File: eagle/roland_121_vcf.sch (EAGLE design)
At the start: 97 parts, among them IC1 LM13700N, IC2 LM13700N, IC3 TL072P, Q1 2N3904, Q2 2N3906, Q3 2N3904, Q4 2N3904, Q5 MPF102, Q6 MPF102, Q7 MPF102, Q8 MPF102

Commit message: starting over with updated techniques
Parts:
- removed C12, C14: 22uF, rcl:CPOL-USB45181A
- removed C18: 0.1uF, rcl:C-US025-030X050
- removed C2: 470p, rcl:C-US025-030X050
- removed R1, R7: 100k, rcl:R-US_0207/7
- removed R18: 10k, rcl:R-US_0207/7
- removed R2, R3: 15k, rcl:R-US_0207/7
- removed R4: 560, rcl:R-US_0207/7
- removed R41: 68k, rcl:R-US_0207/7
- removed U$1: POWER, eurorack:POWER
- added C19: 10/25v BP, rcl:CPOL-USB45181A
- added C21, C22: 10u, rcl:CPOL-USB45181A
- added C23, C24: 100n, rcl:C-US050-024X044
- added FB1, FB2: FB, adafruit:FB
- added FREQ_TRIM: 100k, rcl:R-TRIMM64W
- added R53: 560, rcl:R-US_0207/7
- added R55: 68k, rcl:R-US_0207/7
- added R56: 15k, rcl:R-US_0207/7
- added R57: 22k, rcl:R-US_0207/7
- added R58: 10k, rcl:R-US_0207/7
- added U1: POWER, eurorack:POWER
- added WIDTH: 10k, rcl:R-TRIMM64W
- C1, C11, C13: value 22uF -> 10/25v BP
- C10, C9: value 22uF -> 470p; device rcl:CPOL-USB45181A -> rcl:C-US025-030X050
- C15, C16: value 0.1uF -> 470p
- C17: value 0.1uF -> 10/25v BP; device rcl:C-US025-030X050 -> rcl:CPOL-USB45181A
- C3, C4, C5: value 470p -> 0.1uF
- C6, C7, C8: value 22uF -> 0.1uF; device rcl:CPOL-USB45181A -> rcl:C-US025-030X050
- CUTOFF, CV1_LEVEL, CV2_LEVEL: value 100k -> 100k(B)
- IC1: value LM13700N -> TL072P; device synthdiy updated imperial:LM13700N -> linear:TL072P
- IC3: value TL072P -> LM13700N; device linear:TL072P -> synthdiy updated imperial:LM13700N
- IN1_LEVEL, IN2_LEVEL, RESONANCE: value 100k -> 100k(A)
- Q1, Q4: value 2N3904 -> MPF102; device transistor-npn:2N3904 -> mes_transistors:MPF102
- Q2: value 2N3906 -> 2N3904; device transistor-pnp:2N3906 -> transistor-npn:2N3904
- Q3: value 2N3904 -> 2N3906; device transistor-npn:2N3904 -> transistor-pnp:2N3906
- Q5, Q8: value MPF102 -> 2N3904; device mes_transistors:MPF102 -> transistor-npn:2N3904
- R10: value 33k -> 100k
- R11, R30: value 15k -> 100k
- R12: value 10k -> 1M
- R13: value 10k -> 270k; device rcl:R-TRIMM64W -> rcl:R-US_0207/7
- R15: value 290k -> 10k
- R16: value 100k -> 15k; device rcl:R-TRIMM64W -> rcl:R-US_0207/7
- R17: value 1M -> 27k
- R19: value 1k8 -> 33k
- R20: value 5k6 -> 560
- R22: value 1k5 -> 560
- R23: value 100k -> 1k8
- R24: value 560 -> 5k6
- R25: value 560 -> 10k TEMPCO
- R27: value 22k -> 15k
- R28: value 68k -> 1k5
- R31: value 560 -> 68k
- R33, R40: value 68k -> 560
- R34: value 22k -> 6k8
- R35: value 15k -> 68k
- R36: value 560 -> 15k
- R37: value 560 -> 10k
- R38: value 68k -> 22k
- R39: value 22k -> 68k
- R42: value 68k -> 100
- R43: value 4k7 -> 560
- R47: value 10k -> 4k7
- R48: value 100k -> 10k
- R49: value 100 -> 68k
- R5: value 560 -> 100k
- R50: value 10k -> 15k
- R51: value 10k -> 22k
- R52: value 6k8 -> 68k
- R54: value 150k -> 560
- R9: value 27k -> 150k
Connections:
- removed net N$38: C11.-, C6.-
- removed net N$39: C1.-, C12.-
- removed net N$44: Q7.S, R33.1, R34.2, R42.2
- removed net N$46: C6.+, Q5.S, R28.1, R29.2, R41.2
- removed net N$49: C13.-, C14.-
- new net N$61: FB1.1, U1.+12V
- new net N$62: FB2.1, U1.-12V
- net +12V: now also C21.+, C23.1, C3.1, C5.1, C7.1, FB1.2, FREQ_TRIM.E, IC1P.V+, IC3G$5.V+, Q1.D, Q2.C, Q4.D, Q8.C; no longer C15.1, C17.1, IC1G$5.V+, Q1.C, Q4.C, Q5.D, Q8.D, R16.E, U$1.+12V
- net -12V: now also C22.-, C24.2, C4.2, C6.2, C8.2, FB2.2, FREQ_TRIM.A, IC1P.V-, IC3G$5.V-, R13.2, R30.2, R38.1, R47.2, R51.1, R57.1, R58.1; no longer C16.2, C18.2, IC1G$5.V-, R15.2, R16.A, R23.2, R27.1, R34.1, R39.1, R43.2, R47.1, U$1.-12V
- net GND: now also C10.2, C16.2, C21.-, C22.+, C23.2, C24.1, C4.1, C6.1, C7.2, C8.1, C9.2, IC3G$3.IN, IC3G$4.IN, Q3.E, R15.2, R20.1, R22.1, R28.2, R33.1, R37.2, R40.1, R42.2, R43.1, R53.1, R54.1, U1.GND; no longer C16.1, C17.2, C18.1, C2.2, C4.2, IC1G$3.IN, IC1G$4.IN, Q2.E, R18.2, R22.2, R24.1, R25.1, R31.1, R36.1, R37.1, R4.1, R49.2, R5.1, R50.2, U$1.GND
- net N$1: now also IC2A.IABC, R27.2; no longer IC1A.IABC, R2.2
- net N$10: now also R11.2; no longer R8.2
- net N$11: now also IC1A.+IN; no longer IC3A.+IN
- net N$12: now also IC1B.+IN, R15.1; no longer IC3B.+IN, R18.1
- net N$13: now also IC1B.OUT, R21.2, WIDTH.A, WIDTH.S; no longer IC3B.OUT, R12.2, R13.A, R13.S
- net N$14: now also IC3A.IABC, R50.2; no longer IC2A.IABC, R30.2
- net N$15: now also IC3A.-IN, R39.1, R40.2, R49.2; no longer IC2A.-IN, R32.2, R33.2, R41.1
- net N$16: now also IC1B.-IN, R10.1, R11.1, R12.1, R13.1, R16.2, R9.1; no longer IC3B.-IN, R11.2, R15.1, R17.1, R48.1, R54.1, R8.1
- net N$17: now also FREQ_TRIM.S, R12.2; no longer R16.S, R17.2
- net N$18: now also R23.1, R25.2; no longer R19.1, R21.2
- net N$19: now also R21.1, R23.2, R24.2; no longer R12.1, R19.2, R20.2
- net N$2: now also IC2B.IABC, R36.2; no longer IC1B.IABC, R3.2
- net N$20: now also Q2.B, R24.1, R25.1, R28.1; no longer Q1.B, R20.1, R21.1, R22.1
- net N$21: now also Q2.E, Q3.B, R30.1; no longer Q1.E, Q2.B, R23.1
- net N$22: now also IC2A.-IN, R19.1, R20.2; no longer IC1A.-IN, R10.1, R25.2
- net N$23: now also IC2A.+IN, R22.2, R34.1; no longer IC1A.+IN, R24.2, R52.1
- net N$24: now also IC3A.+IN, R43.2; no longer IC2A.+IN, R31.2
- net N$25: now also IC3B.IABC, R56.2; no longer IC2B.IABC, R35.2
- net N$26: now also IC3B.-IN, R52.1, R53.2, R55.2; no longer IC2B.-IN, R37.2, R38.2, R42.1
- net N$27: now also IC3B.+IN, R54.2; no longer IC2B.+IN, R36.2
- net N$28: now also Q1.S, R29.2, R31.2; no longer Q6.S, R27.2, R40.2
- net N$29: now also C19.-; no longer C9.+
- net N$3: now also IC2B.-IN, R31.1, R32.2, R35.2; no longer IC1B.-IN, R28.2, R40.1, R5.2
- net N$30: now also C13.-; no longer C10.+
- net N$31: now also Q5.E, R47.1; no longer Q3.E, R43.1
- net N$32: now also C13.+, Q5.C; no longer C7.+, Q3.C
- net N$33: now also C11.-, Q5.B; no longer C11.+, Q3.B
- net N$35: now also C11.+, Q4.S, R35.1, R38.2, R39.2; no longer C14.+, C8.+, Q4.E, R38.1, R47.2
- net N$36: now also C17.+, C19.+, Q8.E, R55.1, R58.2; no longer C8.-, C9.-
- net N$37: now also Q6.S, R49.1, R51.2, R52.2; no longer C10.-, C7.-
- net N$4: now also IC2B.+IN, R33.2; no longer IC1B.+IN, R4.2
- net N$40: now also C9.1, IC2A.OUT, Q1.G; no longer C2.1, IC1A.OUT, Q6.G
- net N$41: now also C10.1, IC2B.OUT, Q4.G; no longer C3.1, IC1B.OUT, Q5.G
- net N$42: now also C15.1, IC3A.OUT, Q6.G; no longer C4.1, IC2A.OUT, Q7.G
- net N$43: now also C16.1, IC3B.OUT, Q7.G; no longer C5.1, IC2B.OUT, Q8.G
- net N$45: now also Q3.C, R27.1, R36.1, R50.1, R56.1; no longer Q2.C, R2.1, R3.1, R30.1, R35.1
- net N$47: now also Q7.S, Q8.B, R57.2; no longer Q4.B, Q8.S, R39.2
- net N$48: now also R42.1; no longer R49.1
- net N$5: now also IN2_LEVEL.S, R5.2; no longer IN1_LEVEL.S, R7.2
- net N$50: now also C17.-, R48.2; no longer C13.+, R51.2
- net N$51: now also R48.1; no longer R51.1
- net N$52: now also R34.2, R37.1; no longer R50.1, R52.2
- net N$53: now also R10.2; no longer R48.2
- net N$55: now also U1.CV; no longer U$1.CV
- net N$56: now also R9.2; no longer R54.2
- net N$57: now also IN1_LEVEL.S, R8.1; no longer IN2_LEVEL.S, R1.1
- net N$6: now also R5.1, R8.2; no longer R1.2, R7.1
- net N$7: now also C1.-, IC1A.-IN, R17.2; no longer C12.+, IC3A.-IN, R9.2
- net N$8: now also IC1A.OUT, R17.1, R19.2; no longer IC3A.OUT, R10.2, R9.1
- net N$9: now also R16.1, WIDTH.E; no longer R11.1, R13.E
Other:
- moved on the sheet: 12DB_OUT, 24DB_OUT, C1, C11, C13, C15, C16, C3, C4, C5, CUTOFF, CV1_LEVEL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

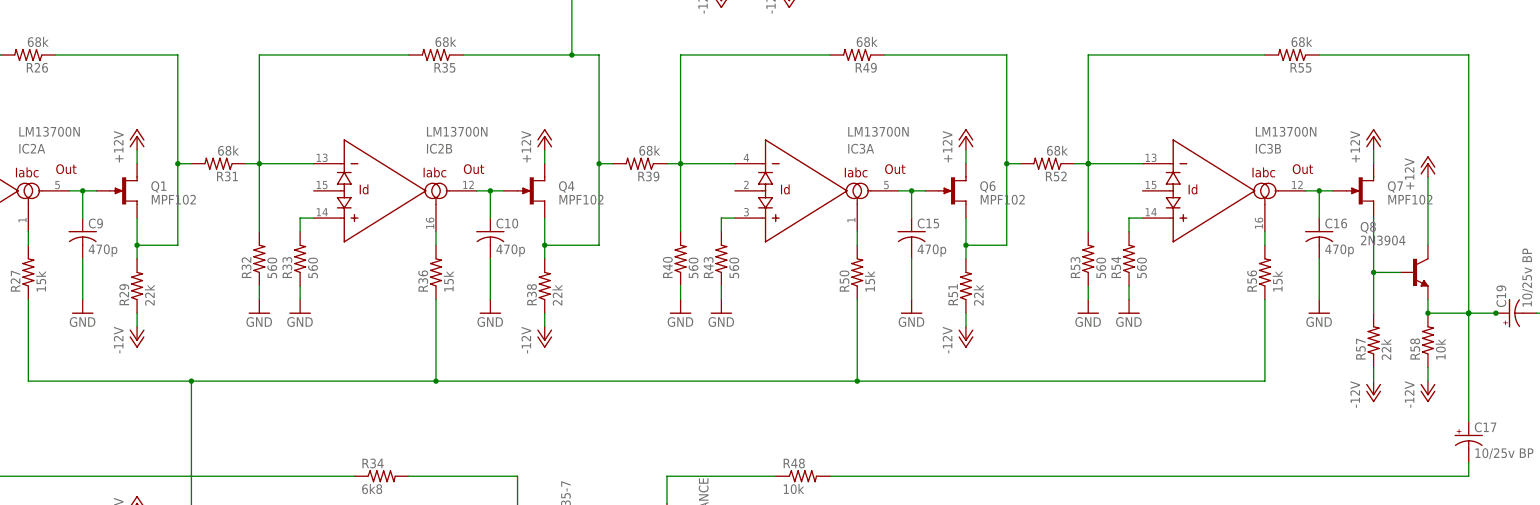
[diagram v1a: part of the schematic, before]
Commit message: changed FET to 2sk30a
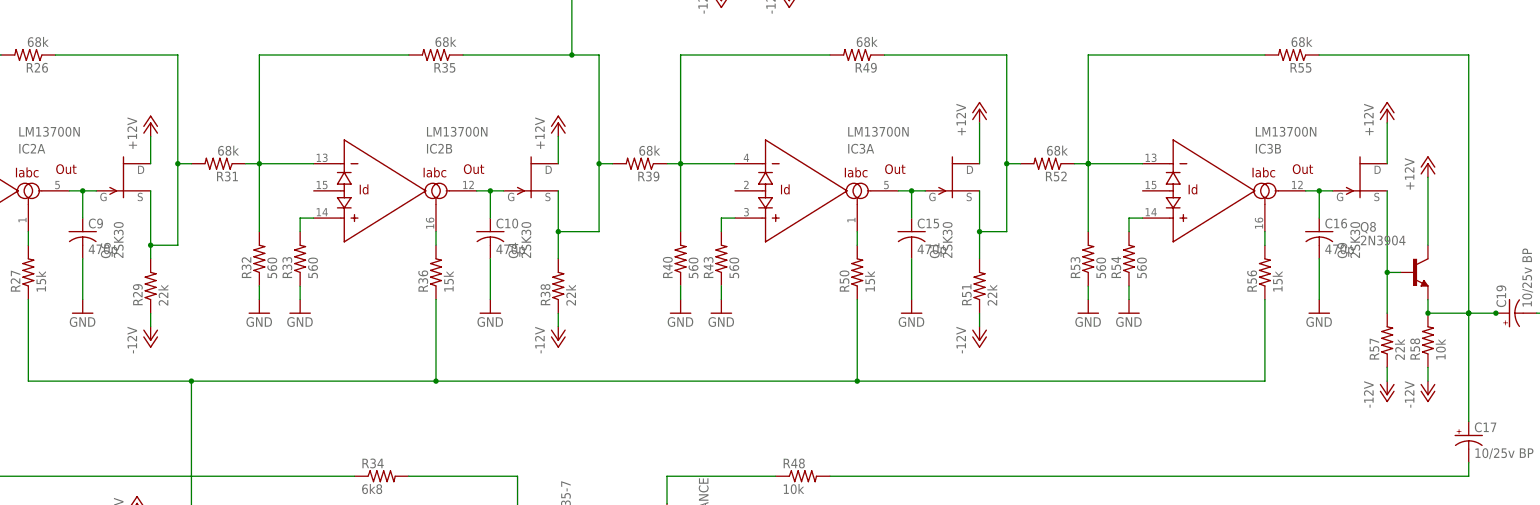
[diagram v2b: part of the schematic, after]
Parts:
- removed Q7: MPF102, mes_transistors:MPF102
- added Q9: 2SK30, 808:2SK30
- Q1, Q4, Q6: value MPF102 -> 2SK30; device mes_transistors:MPF102 -> 808:2SK30
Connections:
- net +12V: now also Q9.D; no longer Q7.D
- net N$28: now also Q6.S; no longer Q1.S
- net N$37: now also Q1.S; no longer Q6.S
- net N$40: now also Q6.G; no longer Q1.G
- net N$42: now also Q1.G; no longer Q6.G
- net N$43: now also Q9.G; no longer Q7.G
- net N$47: now also Q9.S; no longer Q7.S
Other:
- moved on the sheet: R29, R38, R51, R57
